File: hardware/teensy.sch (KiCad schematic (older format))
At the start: 25 parts, among them P5 USB_OTG, SW1 SW_PUSH, U2 LP38691, U3 MKL02Z32, U4 MK20DX256VLH7, Y1 16 MHz, Y2 32.768 kHz

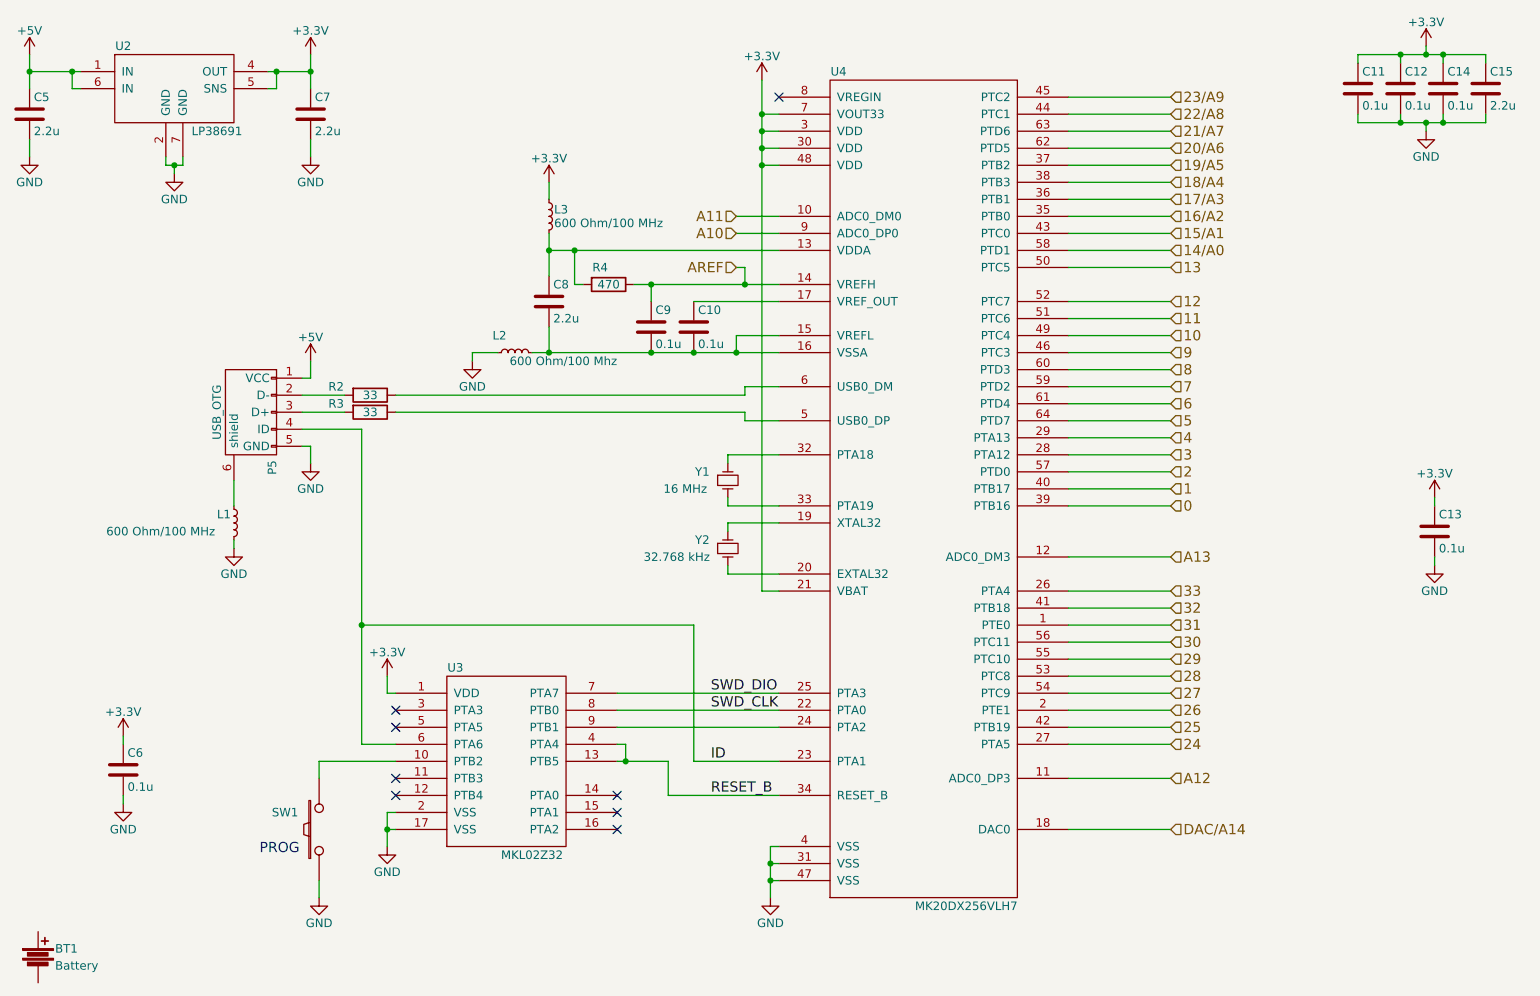
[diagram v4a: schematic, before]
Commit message: Working on capacitive touch pad.  Added footprint for piezo
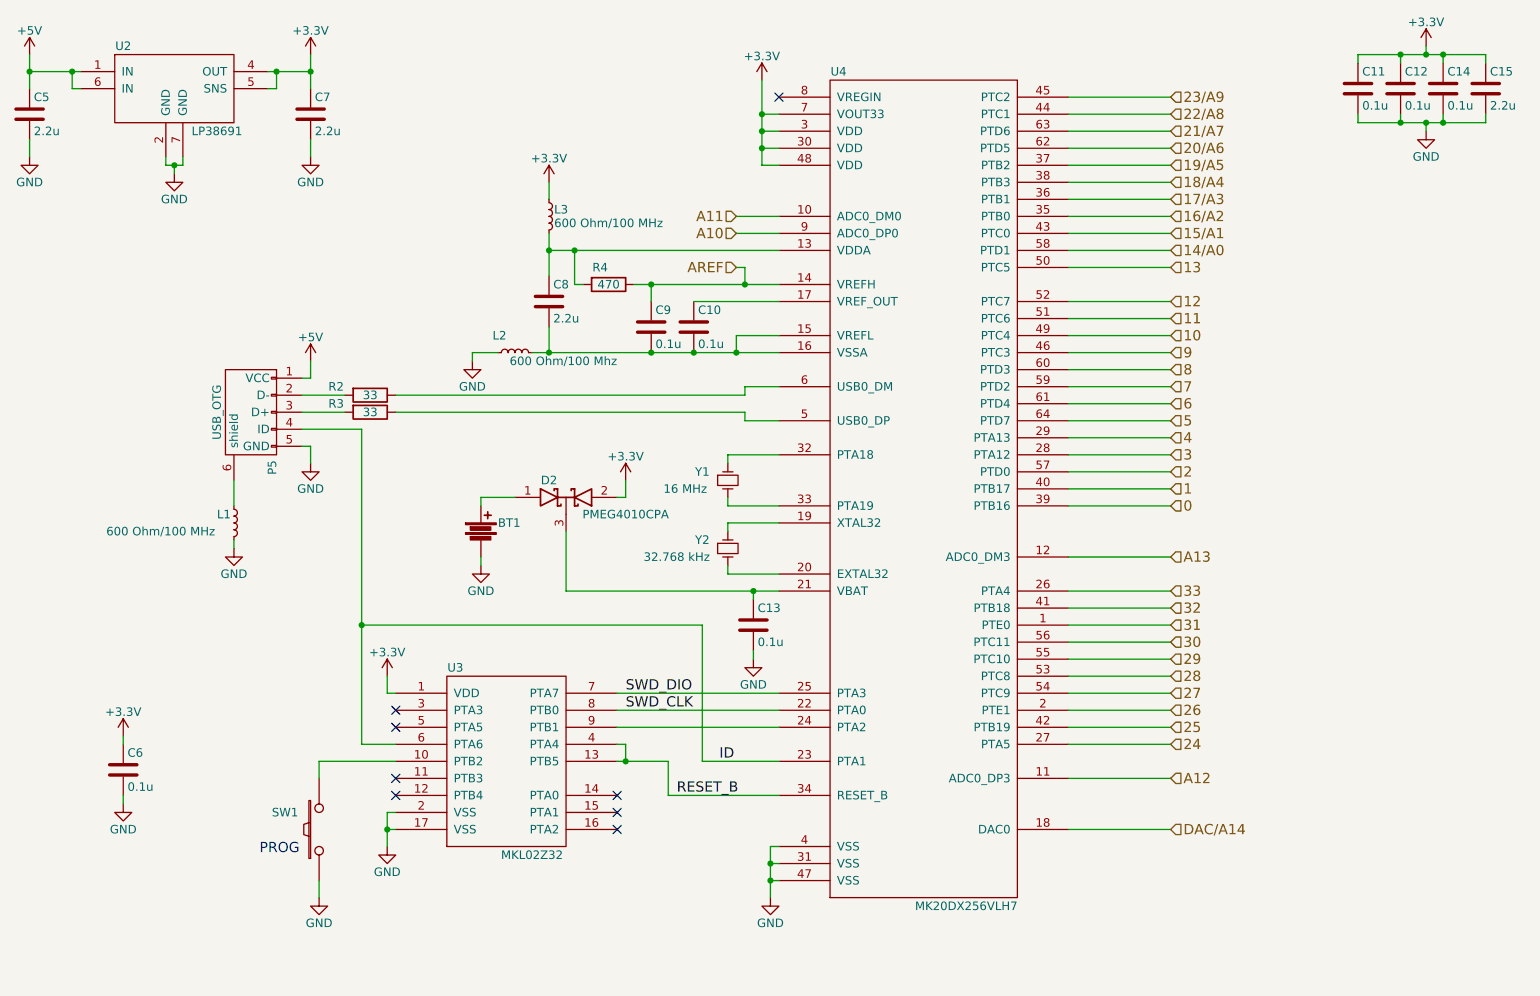
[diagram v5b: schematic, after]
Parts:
- added D2: PMEG4010CPA, symbol D_Schottky_x2_KCom_AAK
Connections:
- net +3V3: now also D2.2 (A); no longer C13.1, U4.21 (VBAT)
- net GND: now also BT1.2
- net at BT1.1: now also D2.1 (A)
- new net: C13.1, D2.3 (K), U4.21 (VBAT)
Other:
- moved on the sheet: BT1, C13
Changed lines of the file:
@@
 $EndDescr
-$Comp
-L MK20DX256VLH7 U4
-U 1 1 57630F8F
-P 6700 2950
-F 0 "U4" H 6200 4750 50  0000 C CNN
-F 1 "MK20DX256VLH7" H 6950 -150 50  0000 C CNN
-F 2 "Housings_QFP:LQFP-64_10x10mm_Pitch0.5mm" H 6550 3050 50  0001 C CNN
-F 3 "DOCUMENTATION" H 6700 2950 50  0001 C CNN
-	1    6700 2950
-	1    0    0    -1
-$EndComp
 $Comp
 L MKL02Z32 U3
@@
 $EndComp
 $Comp
-L GND #PWR35
+L GND #PWR38
 U 1 1 57630FC2
 P 5800 6000
-F 0 "#PWR35" H 5800 5750 50  0001 C CNN
+F 0 "#PWR38" H 5800 5750 50  0001 C CNN
 F 1 "GND" H 5800 5850 50  0000 C CNN
 F 2 "" H 5800 6000 50  0000 C CNN
@@
 NoConn ~ 4900 5400
 $Comp
-L +3.3V #PWR34
+L +3.3V #PWR37
 U 1 1 57630FE2
 P 5750 1200
-F 0 "#PWR34" H 5750 1050 50  0001 C CNN
+F 0 "#PWR37" H 5750 1050 50  0001 C CNN
 F 1 "+3.3V" H 5750 1340 50  0000 C CNN
 F 2 "" H 5750 1200 50  0000 C CNN
@@
 L C C13
 U 1 1 57631024
-P 9700 3850
-F 0 "C13" H 9725 3950 50  0000 L CNN
-F 1 "0.1u" H 9725 3750 50  0000 L CNN
-F 2 "Capacitors_SMD:C_0603" H 9738 3700 50  0001 C CNN
-F 3 "" H 9700 3850 50  0000 C CNN
-	1    9700 3850
-	1    0    0    -1
-$EndComp
-$Comp
-L GND #PWR39
+P 5700 4400
+F 0 "C13" H 5725 4500 50  0000 L CNN
+F 1 "0.1u" H 5725 4300 50  0000 L CNN
+F 2 "Capacitors_SMD:C_0603" H 5738 4250 50  0001 C CNN
+F 3 "" H 5700 4400 50  0000 C CNN
+	1    5700 4400
+	1    0    0    -1
+$EndComp
+$Comp
+L GND #PWR33
 U 1 1 5763102B
-P 9700 4050
-F 0 "#PWR39" H 9700 3800 50  0001 C CNN
-F 1 "GND" H 9700 3900 50  0000 C CNN
-F 2 "" H 9700 4050 50  0000 C CNN
-F 3 "" H 9700 4050 50  0000 C CNN
-	1    9700 4050
-	1    0    0    -1
-$EndComp
-$Comp
-L +3.3V #PWR38
-U 1 1 57631031
-P 9700 3650
-F 0 "#PWR38" H 9700 3500 50  0001 C CNN
-F 1 "+3.3V" H 9700 3790 50  0000 C CNN
-F 2 "" H 9700 3650 50  0000 C CNN
-F 3 "" H 9700 3650 50  0000 C CNN
-	1    9700 3650
+P 4100 4050
+F 0 "#PWR33" H 4100 3800 50  0001 C CNN
+F 1 "GND" H 4100 3900 50  0000 C CNN
+F 2 "" H 4100 4050 50  0000 C CNN
+F 3 "" H 4100 4050 50  0000 C CNN
+	1    4100 4050
 	1    0    0    -1
 $EndComp
@@
 $EndComp
 $Comp
-L +3.3V #PWR33
+L +3.3V #PWR34
 U 1 1 57631075
 P 4500 1800
-F 0 "#PWR33" H 4500 1650 50  0001 C CNN
+F 0 "#PWR34" H 4500 1650 50  0001 C CNN
 F 1 "+3.3V" H 4500 1940 50  0000 C CNN
 F 2 "" H 4500 1800 50  0000 C CNN
@@
 $EndComp
 $Comp
-L +3.3V #PWR36
+L +3.3V #PWR39
 U 1 1 57631098
 P 9650 1000
-F 0 "#PWR36" H 9650 850 50  0001 C CNN
+F 0 "#PWR39" H 9650 850 50  0001 C CNN
 F 1 "+3.3V" H 9650 1140 50  0000 C CNN
 F 2 "" H 9650 1000 50  0000 C CNN
@@
 $EndComp
 $Comp
-L GND #PWR37
+L GND #PWR40
 U 1 1 5763109E
 P 9650 1500
-F 0 "#PWR37" H 9650 1250 50  0001 C CNN
+F 0 "#PWR40" H 9650 1250 50  0001 C CNN
 F 1 "GND" H 9650 1350 50  0000 C CNN
 F 2 "" H 9650 1500 50  0000 C CNN
@@
 Text HLabel 8150 5600 2    60   Input ~ 0
 DAC/A14
-Text Label 5450 5200 0    60   ~ 0
+Text Label 5500 5200 0    60   ~ 0
 ID
-Text Label 5450 4800 0    60   ~ 0
+Text Label 4950 4800 0    60   ~ 0
 SWD_DIO
-Text Label 5450 4900 0    60   ~ 0
+Text Label 4950 4900 0    60   ~ 0
 SWD_CLK
-Text Label 5450 5400 0    60   ~ 0
+Text Label 5250 5400 0    60   ~ 0
 RESET_B
 Text HLabel 5600 2000 0    60   Input ~ 0
@@
 Connection ~ 9750 1450
 Wire Wire Line
-	9750 1400 9750 1450
+	9750 1450 9750 1400
 Connection ~ 9650 1450
 Wire Wire Line
-	9650 1500 9650 1450
+	9650 1450 9650 1500
 Wire Wire Line
 	10000 1450 10000 1400
@@
 Connection ~ 9750 1050
 Wire Wire Line
-	9750 1100 9750 1050
+	9750 1050 9750 1100
 Connection ~ 9650 1050
 Wire Wire Line
@@
 Connection ~ 5600 2800
 Wire Wire Line
-	5600 2700 5600 2800
-Wire Wire Line
-	5850 2700 5600 2700
+	5600 2800 5600 2700
+Wire Wire Line
+	5600 2700 5850 2700
 Wire Wire Line
 	4400 2800 5850 2800
 Wire Wire Line
-	9700 4050 9700 4000
-Wire Wire Line
-	9700 3650 9700 3700
-Wire Wire Line
 	2000 5450 2000 5400
 Wire Wire Line
@@
 Wire Wire Line
 	5850 3800 5550 3800
-Connection ~ 5750 1700
-Wire Wire Line
-	5750 4200 5850 4200
-Connection ~ 5750 1600
-Wire Wire Line
-	5750 1700 5850 1700
-Connection ~ 5750 1500
-Wire Wire Line
-	5750 1600 5850 1600
-Connection ~ 5750 1400
-Wire Wire Line
-	5750 1500 5850 1500
-Wire Wire Line
-	5750 1400 5850 1400
-Wire Wire Line
-	5750 1200 5750 4200
 Wire Wire Line
 	3150 6000 3150 5900
@@
 Connection ~ 5800 5900
 Wire Wire Line
-	5850 5900 5800 5900
+	5800 5900 5850 5900
 Connection ~ 5800 5800
 Wire Wire Line
@@
 	4900 5200 5200 5200
 Wire Wire Line
-	5350 5200 5850 5200
-Wire Wire Line
-	5350 4400 5350 5200
-Wire Wire Line
-	3400 4400 5350 4400
+	5400 5200 5850 5200
+Wire Wire Line
+	5400 4400 5400 5200
+Wire Wire Line
+	3400 4400 5400 4400
 Wire Wire Line
 	5600 2000 5850 2000
@@
 	1450 1050 1450 1250
 Wire Wire Line
-	1750 1150 1450 1150
+	1450 1150 1750 1150
 Connection ~ 1450 1150
 Wire Wire Line
@@
 L Battery BT1
 U 1 1 5766CCF6
-P 1500 6350
-F 0 "BT1" H 1600 6400 50  0000 L CNN
-F 1 "Battery" H 1600 6300 50  0000 L CNN
-F 2 "" V 1500 6390 50  0000 C CNN
-F 3 "" V 1500 6390 50  0000 C CNN
-	1    1500 6350
-	1    0    0    -1
-$EndComp
+P 4100 3850
+F 0 "BT1" H 4200 3900 50  0000 L CNN
+F 1 "Battery" H 4200 3800 50  0001 L CNN
+F 2 "" V 4100 3890 50  0000 C CNN
+F 3 "" V 4100 3890 50  0000 C CNN
+	1    4100 3850
+	1    0    0    -1
+$EndComp
+$Comp
+L MK20DX256VLH7 U4
+U 1 1 57630F8F
+P 6700 2950
+F 0 "U4" H 6200 4750 50  0000 C CNN
+F 1 "MK20DX256VLH7" H 6950 -150 50  0000 C CNN
+F 2 "Housings_QFP:LQFP-64_10x10mm_Pitch0.5mm" H 6550 3050 50  0001 C CNN
+F 3 "DOCUMENTATION" H 6700 2950 50  0001 C CNN
+	1    6700 2950
+	1    0    0    -1
+$EndComp
+Wire Wire Line
+	5750 1700 5850 1700
+Wire Wire Line
+	5750 1200 5750 1700
+Wire Wire Line
+	5850 1400 5750 1400
+Connection ~ 5750 1400
+Wire Wire Line
+	5850 1500 5750 1500
+Connection ~ 5750 1500
+Wire Wire Line
+	5850 1600 5750 1600
+Connection ~ 5750 1600
+$Comp
+L D_Schottky_x2_KCom_AAK D2
+U 1 1 57671962
+P 4600 3650
+F 0 "D2" H 4500 3750 50  0000 C CNN
+F 1 "PMEG4010CPA" H 4950 3550 50  0000 C CNN
+F 2 "" H 4600 3650 50  0000 C CNN
+F 3 "" H 4600 3650 50  0000 C CNN
+	1    4600 3650
+	1    0    0    -1
+$EndComp
+$Comp
+L GND #PWR36
+U 1 1 57671E49
+P 5700 4600
+F 0 "#PWR36" H 5700 4350 50  0001 C CNN
+F 1 "GND" H 5700 4450 50  0000 C CNN
+F 2 "" H 5700 4600 50  0000 C CNN
+F 3 "" H 5700 4600 50  0000 C CNN
+	1    5700 4600
+	1    0    0    -1
+$EndComp
+Wire Wire Line
+	4600 4200 5850 4200
+Wire Wire Line
+	5700 4200 5700 4250
+Wire Wire Line
+	5700 4600 5700 4550
+Wire Wire Line
+	4600 3850 4600 4200
+Connection ~ 5700 4200
+Wire Wire Line
+	4300 3650 4100 3650
+Wire Wire Line
+	4100 3650 4100 3700
+Wire Wire Line
+	4100 4050 4100 4000
+$Comp
+L +3.3V #PWR35
+U 1 1 576736EE
+P 4950 3550
+F 0 "#PWR35" H 4950 3400 50  0001 C CNN
+F 1 "+3.3V" H 4950 3690 50  0000 C CNN
+F 2 "" H 4950 3550 50  0000 C CNN
+F 3 "" H 4950 3550 50  0000 C CNN
+	1    4950 3550
+	1    0    0    -1
+$EndComp
+Wire Wire Line
+	4900 3650 4950 3650
+Wire Wire Line
+	4950 3650 4950 3550
 $EndSCHEMATC

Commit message: Added footprint for coin cell battery holder and RJ10 jack
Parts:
- BT1: footprint (none) -> footprint:BK-885
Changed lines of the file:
@@
 F 0 "BT1" H 4200 3900 50  0000 L CNN
 F 1 "Battery" H 4200 3800 50  0001 L CNN
-F 2 "" V 4100 3890 50  0000 C CNN
+F 2 "footprint:BK-885" V 4100 3890 50  0001 C CNN
 F 3 "" V 4100 3890 50  0000 C CNN
 	1    4100 3850

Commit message: Working on footprints.  Exported netlist into layout.
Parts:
- D2: footprint (none) -> footprint:SOT1061
- P5: footprint (none) -> footprint:10118192
- R4: footprint (none) -> Resistors_SMD:R_0603
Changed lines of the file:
@@
 $EndComp
 $Comp
-L GND #PWR31
+L GND #PWR019
 U 1 1 57630FB2
 P 3550 5700
-F 0 "#PWR31" H 3550 5450 50  0001 C CNN
+F 0 "#PWR019" H 3550 5450 50  0001 C CNN
 F 1 "GND" H 3550 5550 50  0000 C CNN
 F 2 "" H 3550 5700 50  0000 C CNN
@@
 $EndComp
 $Comp
-L +3.3V #PWR30
+L +3.3V #PWR020
 U 1 1 57630FBC
 P 3550 4700
-F 0 "#PWR30" H 3550 4550 50  0001 C CNN
+F 0 "#PWR020" H 3550 4550 50  0001 C CNN
 F 1 "+3.3V" H 3550 4840 50  0000 C CNN
 F 2 "" H 3550 4700 50  0000 C CNN
@@
 $EndComp
 $Comp
-L GND #PWR38
+L GND #PWR021
 U 1 1 57630FC2
 P 5800 6000
-F 0 "#PWR38" H 5800 5750 50  0001 C CNN
+F 0 "#PWR021" H 5800 5750 50  0001 C CNN
 F 1 "GND" H 5800 5850 50  0000 C CNN
 F 2 "" H 5800 6000 50  0000 C CNN
@@
 $EndComp
 $Comp
-L GND #PWR29
+L GND #PWR022
 U 1 1 57630FD0
 P 3150 6000
-F 0 "#PWR29" H 3150 5750 50  0001 C CNN
+F 0 "#PWR022" H 3150 5750 50  0001 C CNN
 F 1 "GND" H 3150 5850 50  0000 C CNN
 F 2 "" H 3150 6000 50  0000 C CNN
@@
 NoConn ~ 4900 5400
 $Comp
-L +3.3V #PWR37
+L +3.3V #PWR023
 U 1 1 57630FE2
 P 5750 1200
-F 0 "#PWR37" H 5750 1050 50  0001 C CNN
+F 0 "#PWR023" H 5750 1050 50  0001 C CNN
 F 1 "+3.3V" H 5750 1340 50  0000 C CNN
 F 2 "" H 5750 1200 50  0000 C CNN
@@
 F 0 "P5" H 3075 3025 50  0000 C CNN
 F 1 "USB_OTG" H 2750 3350 50  0000 C CNN
-F 2 "" V 2700 3050 50  0000 C CNN
+F 2 "footprint:10118192" V 2700 3050 50  0001 C CNN
 F 3 "" V 2700 3050 50  0000 C CNN
 	1    2750 3150
@@
 $EndComp
 $Comp
-L GND #PWR22
+L GND #PWR024
 U 1 1 57631016
 P 2000 5450
-F 0 "#PWR22" H 2000 5200 50  0001 C CNN
+F 0 "#PWR024" H 2000 5200 50  0001 C CNN
 F 1 "GND" H 2000 5300 50  0000 C CNN
 F 2 "" H 2000 5450 50  0000 C CNN
@@
 $EndComp
 $Comp
-L +3.3V #PWR21
+L +3.3V #PWR025
 U 1 1 5763101C
 P 2000 5050
-F 0 "#PWR21" H 2000 4900 50  0001 C CNN
+F 0 "#PWR025" H 2000 4900 50  0001 C CNN
 F 1 "+3.3V" H 2000 5190 50  0000 C CNN
 F 2 "" H 2000 5050 50  0000 C CNN
@@
 $EndComp
 $Comp
-L GND #PWR33
+L GND #PWR026
 U 1 1 5763102B
 P 4100 4050
-F 0 "#PWR33" H 4100 3800 50  0001 C CNN
+F 0 "#PWR026" H 4100 3800 50  0001 C CNN
 F 1 "GND" H 4100 3900 50  0000 C CNN
 F 2 "" H 4100 4050 50  0000 C CNN
@@
 F 0 "R4" V 4750 2350 50  0000 C CNN
 F 1 "470" V 4850 2400 50  0000 C CNN
-F 2 "" V 4780 2400 50  0000 C CNN
+F 2 "Resistors_SMD:R_0603" V 4780 2400 50  0001 C CNN
 F 3 "" H 4850 2400 50  0000 C CNN
 	1    4850 2400
@@
 $EndComp
 $Comp
-L GND #PWR32
+L GND #PWR027
 U 1 1 57631066
 P 4050 2850
-F 0 "#PWR32" H 4050 2600 50  0001 C CNN
+F 0 "#PWR027" H 4050 2600 50  0001 C CNN
 F 1 "GND" H 4050 2700 50  0000 C CNN
 F 2 "" H 4050 2850 50  0000 C CNN
@@
 $EndComp
 $Comp
-L +3.3V #PWR34
+L +3.3V #PWR028
 U 1 1 57631075
 P 4500 1800
-F 0 "#PWR34" H 4500 1650 50  0001 C CNN
+F 0 "#PWR028" H 4500 1650 50  0001 C CNN
 F 1 "+3.3V" H 4500 1940 50  0000 C CNN
 F 2 "" H 4500 1800 50  0000 C CNN
@@
 $EndComp
 $Comp
-L +3.3V #PWR39
+L +3.3V #PWR029
 U 1 1 57631098
 P 9650 1000
-F 0 "#PWR39" H 9650 850 50  0001 C CNN
+F 0 "#PWR029" H 9650 850 50  0001 C CNN
 F 1 "+3.3V" H 9650 1140 50  0000 C CNN
 F 2 "" H 9650 1000 50  0000 C CNN
@@
 $EndComp
 $Comp
-L GND #PWR40
+L GND #PWR030
 U 1 1 5763109E
 P 9650 1500
-F 0 "#PWR40" H 9650 1250 50  0001 C CNN
+F 0 "#PWR030" H 9650 1250 50  0001 C CNN
 F 1 "GND" H 9650 1350 50  0000 C CNN
 F 2 "" H 9650 1500 50  0000 C CNN
@@
 $EndComp
 $Comp
-L GND #PWR24
+L GND #PWR031
 U 1 1 57632880
 P 2650 3950
-F 0 "#PWR24" H 2650 3700 50  0001 C CNN
+F 0 "#PWR031" H 2650 3700 50  0001 C CNN
 F 1 "GND" H 2650 3800 50  0000 C CNN
 F 2 "" H 2650 3950 50  0000 C CNN
@@
 $EndComp
 $Comp
-L GND #PWR28
+L GND #PWR032
 U 1 1 576328C7
 P 3100 3450
-F 0 "#PWR28" H 3100 3200 50  0001 C CNN
+F 0 "#PWR032" H 3100 3200 50  0001 C CNN
 F 1 "GND" H 3100 3300 50  0000 C CNN
 F 2 "" H 3100 3450 50  0000 C CNN
@@
 $EndComp
 $Comp
-L +5V #PWR27
+L +5V #PWR033
 U 1 1 5763FF76
 P 3100 2850
-F 0 "#PWR27" H 3100 2700 50  0001 C CNN
+F 0 "#PWR033" H 3100 2700 50  0001 C CNN
 F 1 "+5V" H 3100 2990 50  0000 C CNN
 F 2 "" H 3100 2850 50  0000 C CNN
@@
 $EndComp
 $Comp
-L +5V #PWR19
+L +5V #PWR034
 U 1 1 57640ACB
 P 1450 1050
-F 0 "#PWR19" H 1450 900 50  0001 C CNN
+F 0 "#PWR034" H 1450 900 50  0001 C CNN
 F 1 "+5V" H 1450 1190 50  0000 C CNN
 F 2 "" H 1450 1050 50  0000 C CNN
@@
 $EndComp
 $Comp
-L +3.3V #PWR25
+L +3.3V #PWR035
 U 1 1 57641034
 P 3100 1050
-F 0 "#PWR25" H 3100 900 50  0001 C CNN
+F 0 "#PWR035" H 3100 900 50  0001 C CNN
 F 1 "+3.3V" H 3100 1190 50  0000 C CNN
 F 2 "" H 3100 1050 50  0000 C CNN
@@
 $EndComp
 $Comp
-L GND #PWR26
+L GND #PWR036
 U 1 1 57641148
 P 3100 1650
-F 0 "#PWR26" H 3100 1400 50  0001 C CNN
+F 0 "#PWR036" H 3100 1400 50  0001 C CNN
 F 1 "GND" H 3100 1500 50  0000 C CNN
 F 2 "" H 3100 1650 50  0000 C CNN
@@
 $EndComp
 $Comp
-L GND #PWR20
+L GND #PWR037
 U 1 1 5764119E
 P 1450 1650
-F 0 "#PWR20" H 1450 1400 50  0001 C CNN
+F 0 "#PWR037" H 1450 1400 50  0001 C CNN
 F 1 "GND" H 1450 1500 50  0000 C CNN
 F 2 "" H 1450 1650 50  0000 C CNN
@@
 $EndComp
 $Comp
-L GND #PWR23
+L GND #PWR038
 U 1 1 576416D5
 P 2300 1750
-F 0 "#PWR23" H 2300 1500 50  0001 C CNN
+F 0 "#PWR038" H 2300 1500 50  0001 C CNN
 F 1 "GND" H 2300 1600 50  0000 C CNN
 F 2 "" H 2300 1750 50  0000 C CNN
@@
 F 0 "D2" H 4500 3750 50  0000 C CNN
 F 1 "PMEG4010CPA" H 4950 3550 50  0000 C CNN
-F 2 "" H 4600 3650 50  0000 C CNN
+F 2 "footprint:SOT1061" H 4600 3650 50  0001 C CNN
 F 3 "" H 4600 3650 50  0000 C CNN
 	1    4600 3650
@@
 $EndComp
 $Comp
-L GND #PWR36
+L GND #PWR039
 U 1 1 57671E49
 P 5700 4600
-F 0 "#PWR36" H 5700 4350 50  0001 C CNN
+F 0 "#PWR039" H 5700 4350 50  0001 C CNN
 F 1 "GND" H 5700 4450 50  0000 C CNN
 F 2 "" H 5700 4600 50  0000 C CNN
@@
 	4100 4050 4100 4000
 $Comp
-L +3.3V #PWR35
+L +3.3V #PWR040
 U 1 1 576736EE
 P 4950 3550
-F 0 "#PWR35" H 4950 3400 50  0001 C CNN
+F 0 "#PWR040" H 4950 3400 50  0001 C CNN
 F 1 "+3.3V" H 4950 3690 50  0000 C CNN
 F 2 "" H 4950 3550 50  0000 C CNN

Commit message: Working on PCB layout
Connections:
- net USB_D+: now reaches R3.1, U4.5 (USB0_DP)
- net USB_D-: now reaches R2.1, U4.6 (USB0_DM)
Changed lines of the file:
@@
 Wire Wire Line
 	4950 3650 4950 3550
+Text Label 4400 3050 0    60   ~ 0
+USB_D-
+Text Label 4400 3150 0    60   ~ 0
+USB_D+
 $EndSCHEMATC
